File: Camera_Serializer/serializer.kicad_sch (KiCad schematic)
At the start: 1 part

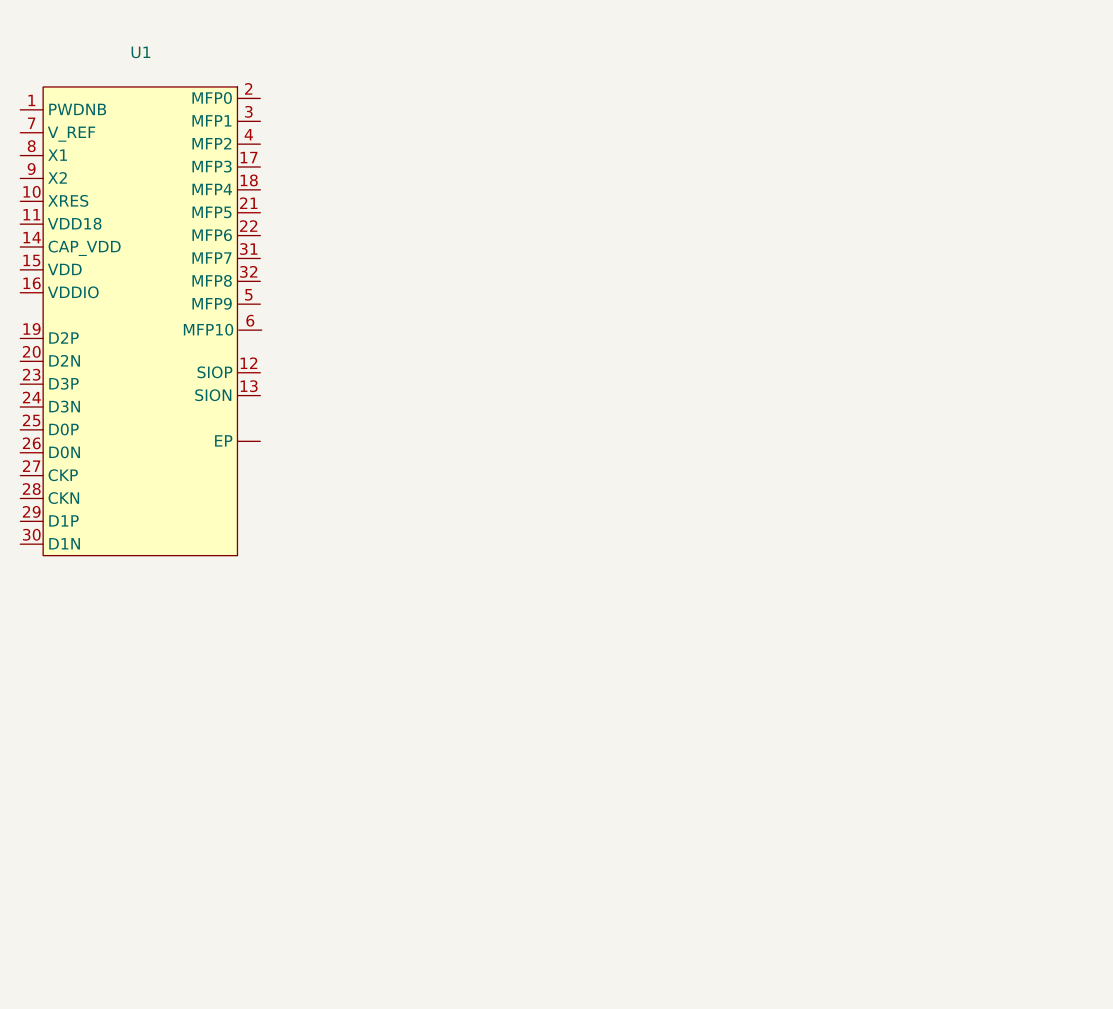
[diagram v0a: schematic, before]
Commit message: Added serializer schematic and fakra connector
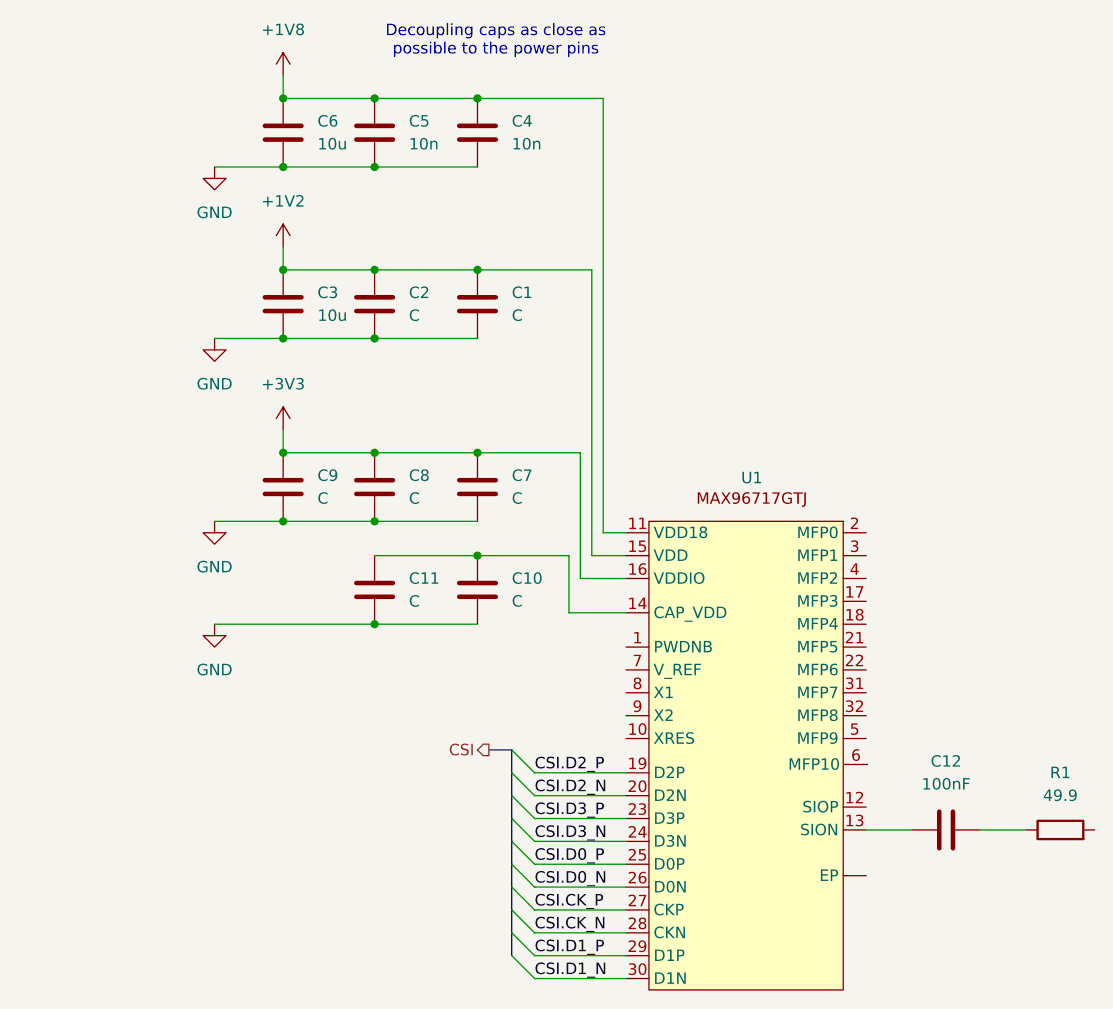
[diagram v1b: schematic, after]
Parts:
- added C1, C10, C11, C2, C7, C8, C9: C, symbol Device:C
- added C12: 100nF, symbol Device:C
- added C3, C6: 10u, symbol Device:C
- added C4, C5: 10n, symbol Device:C
- added R1: 49.9, symbol Device:R
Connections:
- net +1V8: now reaches U1.11 (VDD18)
- net +1V8: now also C4.1, C5.1, C6.1
- net at U1.13 (SION): now also C12.1
- net at U1.14 (CAP_VDD): now also C10.1, C11.1
- net +1V2: now reaches U1.15 (VDD)
- net +1V2: now also C1.1, C2.1, C3.1
- net +3V3: now reaches U1.16 (VDDIO)
- net +3V3: now also C7.1, C8.1, C9.1
- net CSI.D2_P: now reaches U1.19 (D2P)
- net CSI.D2_N: now reaches U1.20 (D2N)
- net CSI.D3_P: now reaches U1.23 (D3P)
- net CSI.D3_N: now reaches U1.24 (D3N)
- net CSI.D0_P: now reaches U1.25 (D0P)
- net CSI.D0_N: now reaches U1.26 (D0N)
- net CSI.CK_P: now reaches U1.27 (CKP)
- net CSI.CK_N: now reaches U1.28 (CKN)
- net CSI.D1_P: now reaches U1.29 (D1P)
- net CSI.D1_N: now reaches U1.30 (D1N)
- new net: C12.2, R1.1
- new net GND: C1.2, C10.2, C11.2, C2.2, C3.2, C4.2, C5.2, C6.2, C7.2, C8.2, C9.2
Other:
- note added: "Decoupling caps as close as possible to the power pins"

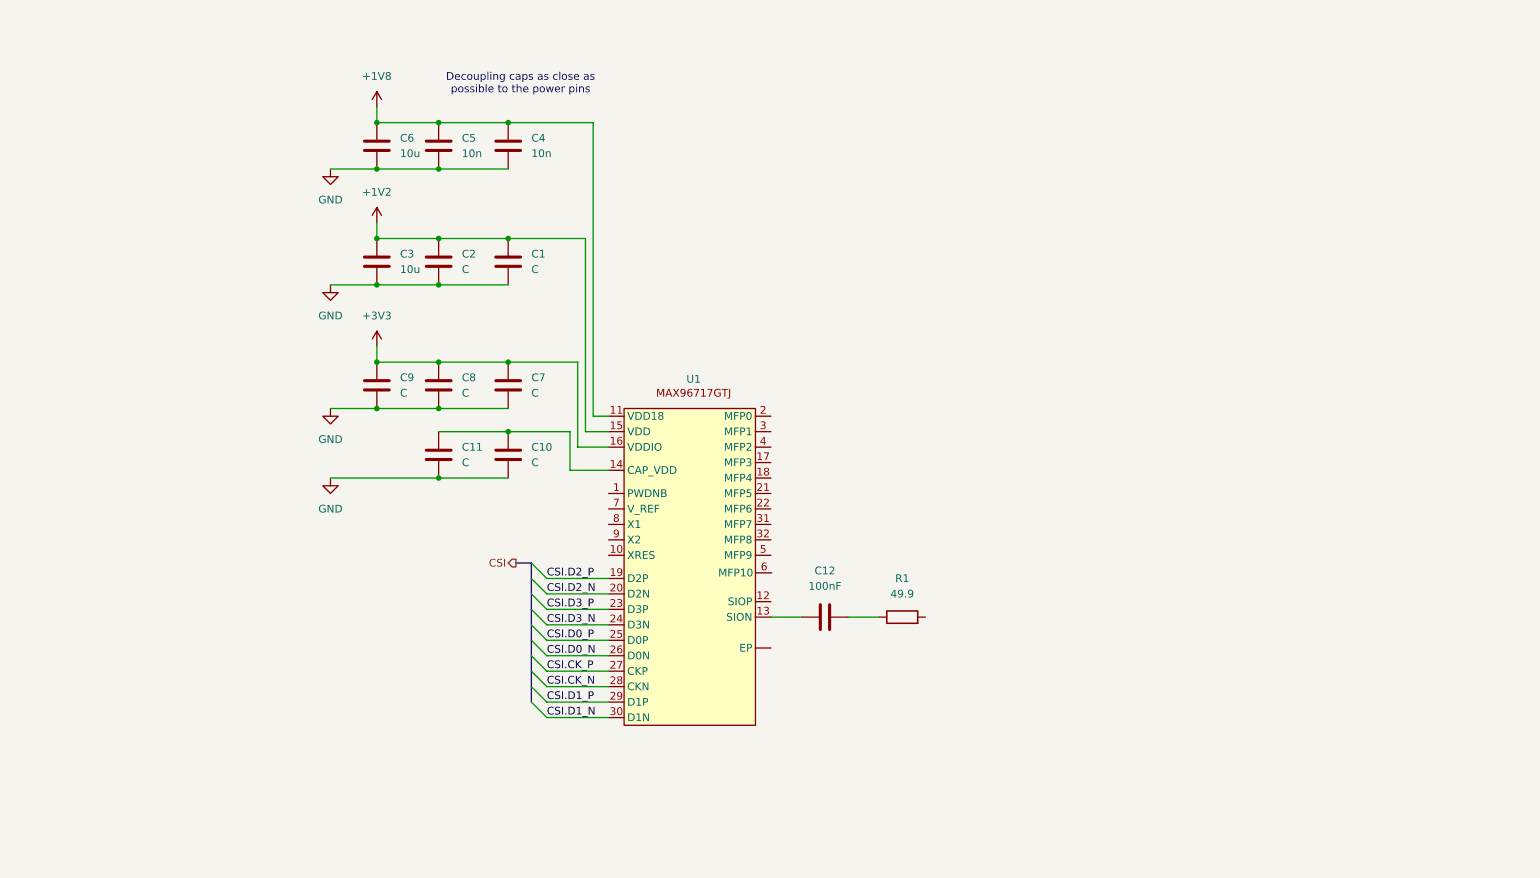
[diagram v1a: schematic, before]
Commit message: Added crystal and capacitor, plus config resistors
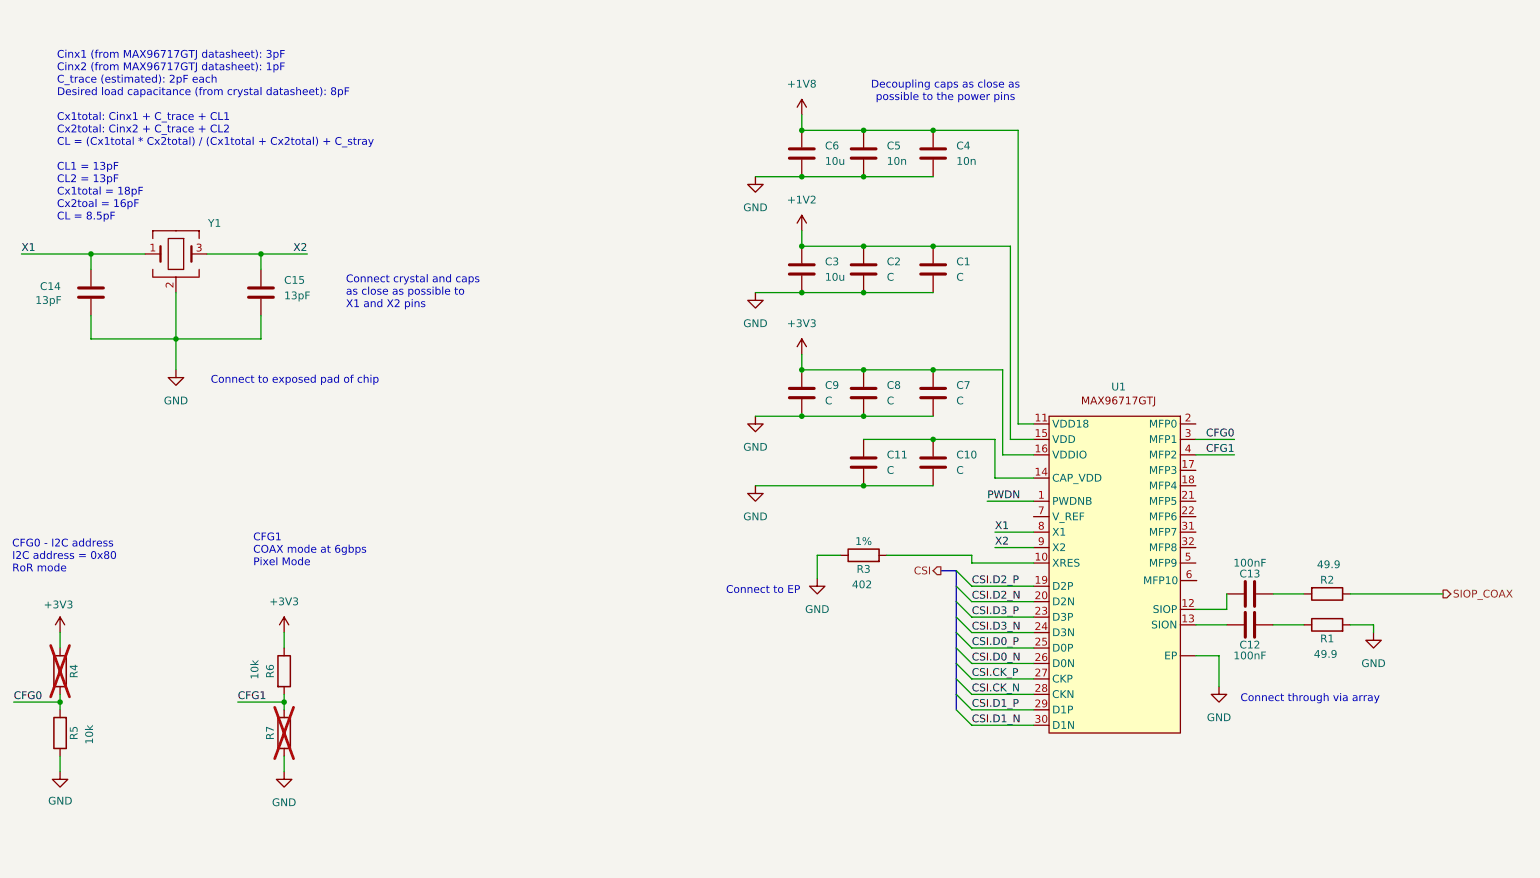
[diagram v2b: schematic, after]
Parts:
- added C13: 100nF, Capacitor_SMD:C_0402_1005Metric, symbol Device:C
- added C14, C15: 13pF, Capacitor_SMD:C_0402_1005Metric, symbol Device:C
- added R2: 49.9, symbol Device:R
- added R3: 402, Resistor_SMD:R_0402_1005Metric, symbol Device:R
- added R4, R7: ~, symbol Device:R
- added R5: 10k, Resistor_SMD:R_0402_1005Metric, symbol Device:R
- added R6: 10k, symbol Device:R
- added Y1: ~, symbol EB2532YA08-25.000M_TR:EB2532YA08-25.000M_TR
- C12: footprint (none) -> Capacitor_SMD:C_0402_1005Metric
- R1: footprint (none) -> Resistor_SMD:R_0402_1005Metric
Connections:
- net +3V3: now also R4.2, R6.1
- net GND: now also R1.2, U1. (EP), C14.2, C15.2, R3.1, R5.1, R7.2, Y1.2
- net at C12.1: now also R1.1; no longer U1.13 (SION)
- net at C12.2: now also U1.13 (SION); no longer R1.1
- net PWDN: now reaches U1.1 (PWDNB)
- net at U1.10 (XRES): now also R3.2
- net at U1.12 (SIOP): now also C13.1
- net CFG0: now reaches U1.3 (MFP1)
- net CFG0: now also R4.1, R5.2
- net CFG1: now reaches U1.4 (MFP2)
- net CFG1: now also R6.2, R7.1
- net X1: now reaches U1.8 (X1)
- net X1: now also C14.1, Y1.1
- net X2: now reaches U1.9 (X2)
- net X2: now also C15.1, Y1.3
- new net: C13.2, R2.2
- new net SIOP_COAX: R2.1
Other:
- note added: "CFG0 - I2C address I2C address = 0x80 RoR mode"
- note added: "CFG1 COAX mode at 6gbps Pixel Mode"
- note added: "Cinx1 (from MAX96717GTJ datasheet): 3pF Cinx2 (from MAX96717GTJ datasheet): 1pF C_trace (estimated): 2pF each Desired load capacitance (from crystal datasheet): 8pF Cx1total: Cinx1 + C_trace + CL1 Cx2total: Cinx2 + C_trace + CL2 CL = (Cx1total * Cx2total) / (Cx1total + Cx2total) + C_stray CL1 = 13pF CL2 = 13pF Cx1total = 18pF Cx2toal = 16pF CL = 8.5pF"
- note added: "Connect crystal and caps as close as possible to X1 and X2 pins"
- note added: "Connect through via array"
- note added: "Connect to EP"
- note added: "Connect to exposed pad of chip"
- moved on the sheet: C1, C10, C11, C12, C2, C3, C4, C5, C6, C7, C8, C9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

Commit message: Basic setup of main SOC done, working on POC circuit now.
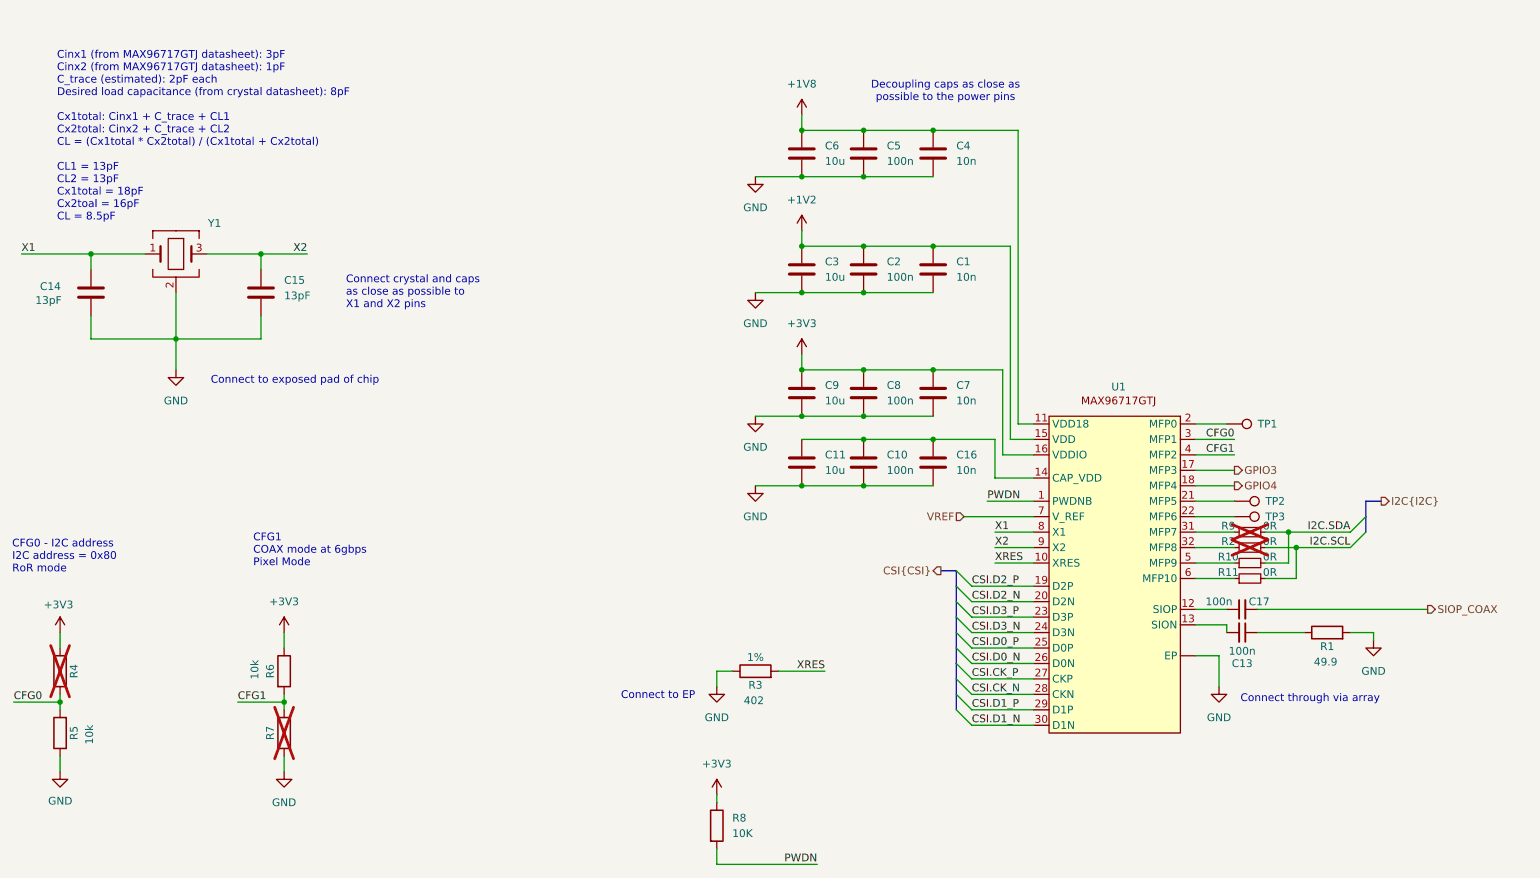
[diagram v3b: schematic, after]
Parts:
- removed C12, C13: 100nF, Capacitor_SMD:C_0402_1005Metric, symbol Device:C
- removed R2: 49.9, symbol Device:R
- added C13, C17: 100n, symbol Device:C_Small
- added C16: 10n, symbol Device:C
- added R10, R11, R2, R9: 0R, symbol Device:R_Small
- added R8: 10K, symbol Device:R
- added TP1, TP2, TP3: TestPoint, symbol Connector:TestPoint
- C1, C7: value C -> 10n
- C10, C2, C8: value C -> 100n
- C11, C9: value C -> 10u
- C5: value 10n -> 100n
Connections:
- net +3V3: now also R8.1
- net GND: now also C16.2
- net PWDN: now also R8.2
- net SIOP_COAX: now also C17.2
- net at C10.1, C11.1, U1.14 (CAP_VDD): now also C16.1
- net at R1.1: now also C13.1
- net at U1.13 (SION): now also C13.2
- net XRES: now reaches R3.2, U1.10 (XRES)
- net at U1.12 (SIOP): now also C17.1
- net GPIO3: now reaches U1.17 (MFP3)
- net GPIO4: now reaches U1.18 (MFP4)
- net at U1.2 (MFP0): now also TP1.1
- net at U1.21 (MFP5): now also TP2.1
- net at U1.22 (MFP6): now also TP3.1
- net at U1.31 (MFP7): now also R9.1
- net at U1.32 (MFP8): now also R2.1
- net at U1.5 (MFP9): now also R10.1
- net at U1.6 (MFP10): now also R11.1
- net VREF: now reaches U1.7 (V_REF)
- new net I2C.SCL: R11.2, R2.2
- new net I2C.SDA: R10.2, R9.2
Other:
- note added: "Cinx1 (from MAX96717GTJ datasheet): 3pF Cinx2 (from MAX96717GTJ datasheet): 1pF C_trace (estimated): 2pF each Desired load capacitance (from crystal datasheet): 8pF Cx1total: Cinx1 + C_trace + CL1 Cx2total: Cinx2 + C_trace + CL2 CL = (Cx1total * Cx2total) / (Cx1total + Cx2total) CL1 = 13pF CL2 = 13pF Cx1total = 18pF Cx2toal = 16pF CL = 8.5pF"
- note removed: "Cinx1 (from MAX96717GTJ datasheet): 3pF Cinx2 (from MAX96717GTJ datasheet): 1pF C_trace (estimated): 2pF each Desired load capacitance (from crystal datasheet): 8pF Cx1total: Cinx1 + C_trace + CL1 Cx2total: Cinx2 + C_trace + CL2 CL = (Cx1total * Cx2total) / (Cx1total + Cx2total) + C_stray CL1 = 13pF CL2 = 13pF Cx1total = 18pF Cx2toal = 16pF CL = 8.5pF"
- moved on the sheet: C10, C11, R1, R3

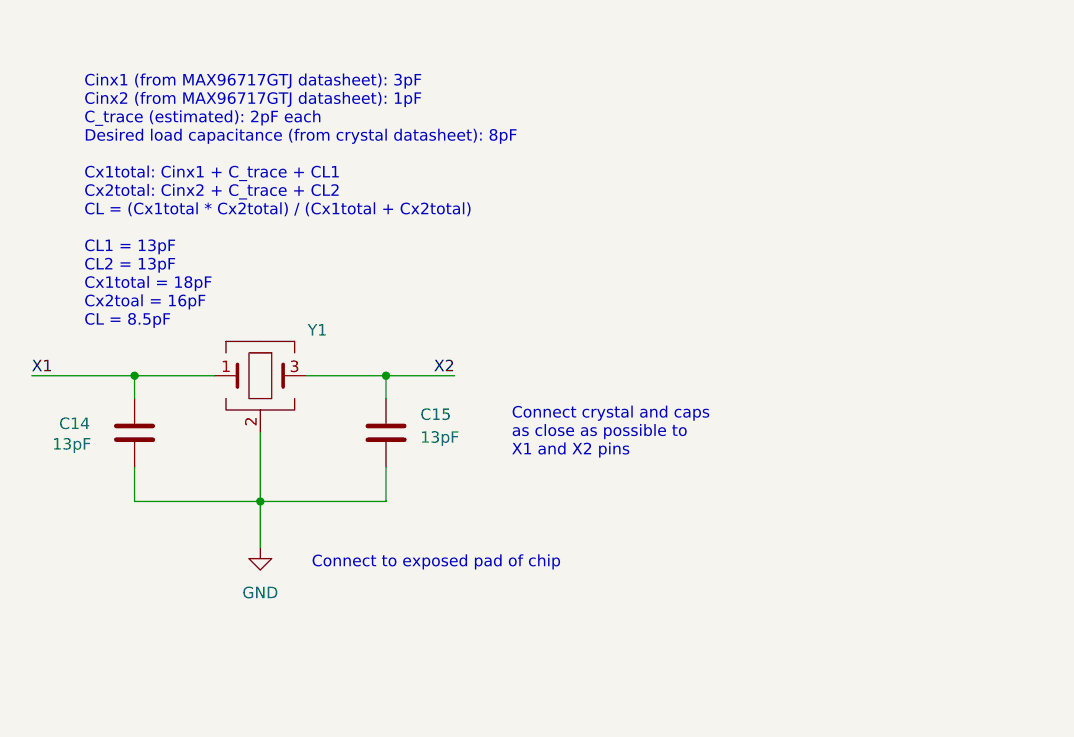
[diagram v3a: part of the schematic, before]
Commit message: Finished POC circuit and added TVS diode
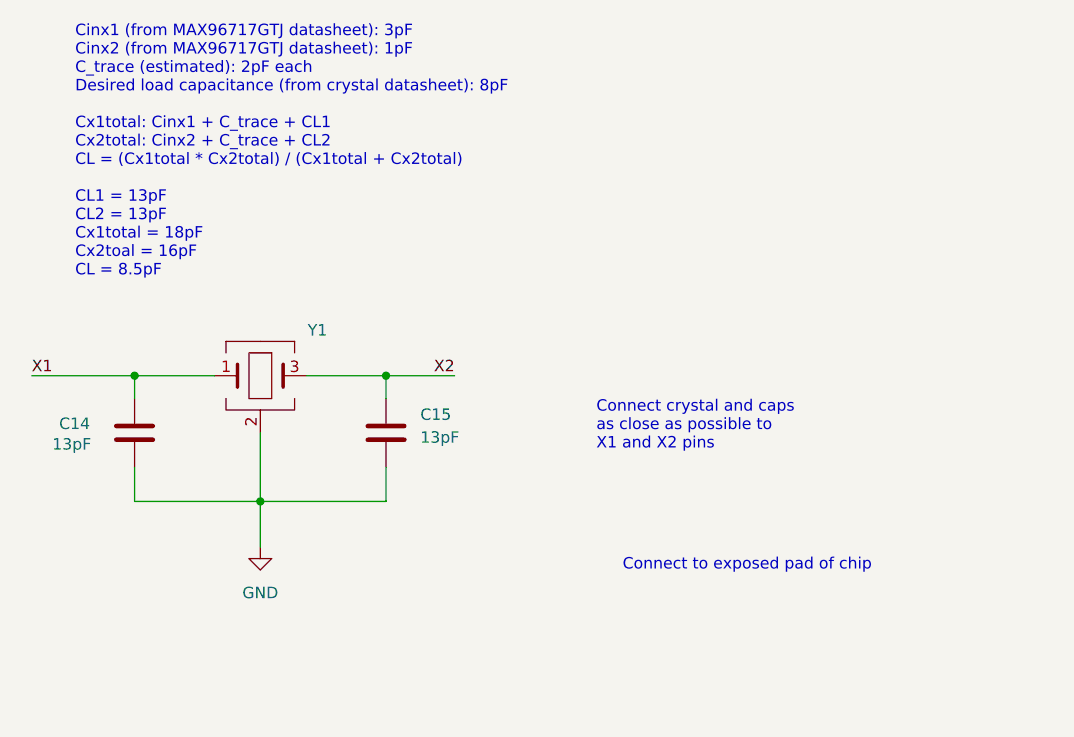
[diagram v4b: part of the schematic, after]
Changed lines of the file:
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@@
 	(text "Connect to exposed pad of chip"
 		(exclude_from_sim no)
-		(at 77.978 76.708 0)
+		(at 112.522 76.962 0)
 		(effects
 			(font
@@
 	(text "Cinx1 (from MAX96717GTJ datasheet): 3pF\nCinx2 (from MAX96717GTJ datasheet): 1pF\nC_trace (estimated): 2pF each\nDesired load capacitance (from crystal datasheet): 8pF\n\nCx1total: Cinx1 + C_trace + CL1\nCx2total: Cinx2 + C_trace + CL2\nCL = (Cx1total * Cx2total) / (Cx1total + Cx2total)\n\nCL1 = 13pF\nCL2 = 13pF\nCx1total = 18pF\nCx2toal = 16pF\nCL = 8.5pF"
 		(exclude_from_sim no)
-		(at 38.862 36.576 0)
+		(at 37.846 30.988 0)
 		(effects
 			(font
@@
 	(text "Connect crystal and caps \nas close as possible to \nX1 and X2 pins"
 		(exclude_from_sim no)
-		(at 86.36 62.23 0)
+		(at 95.758 61.468 0)
 		(effects
 			(font
@@
 			)
 		)
-		(property "Datasheet" "https://content.kemet.com/datasheets/KEM_C1030_CBR_SMD.pdf"
+		(property "Datasheet" "~"
 			(at 72.39 62.23 0)
 			(effects
@@
 			)
 		)
-		(property "Datasheet" "https://content.kemet.com/datasheets/KEM_C1030_CBR_SMD.pdf"
+		(property "Datasheet" "~"
 			(at 44.45 62.23 0)
 			(effects
